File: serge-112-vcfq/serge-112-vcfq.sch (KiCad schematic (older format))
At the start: 90 parts

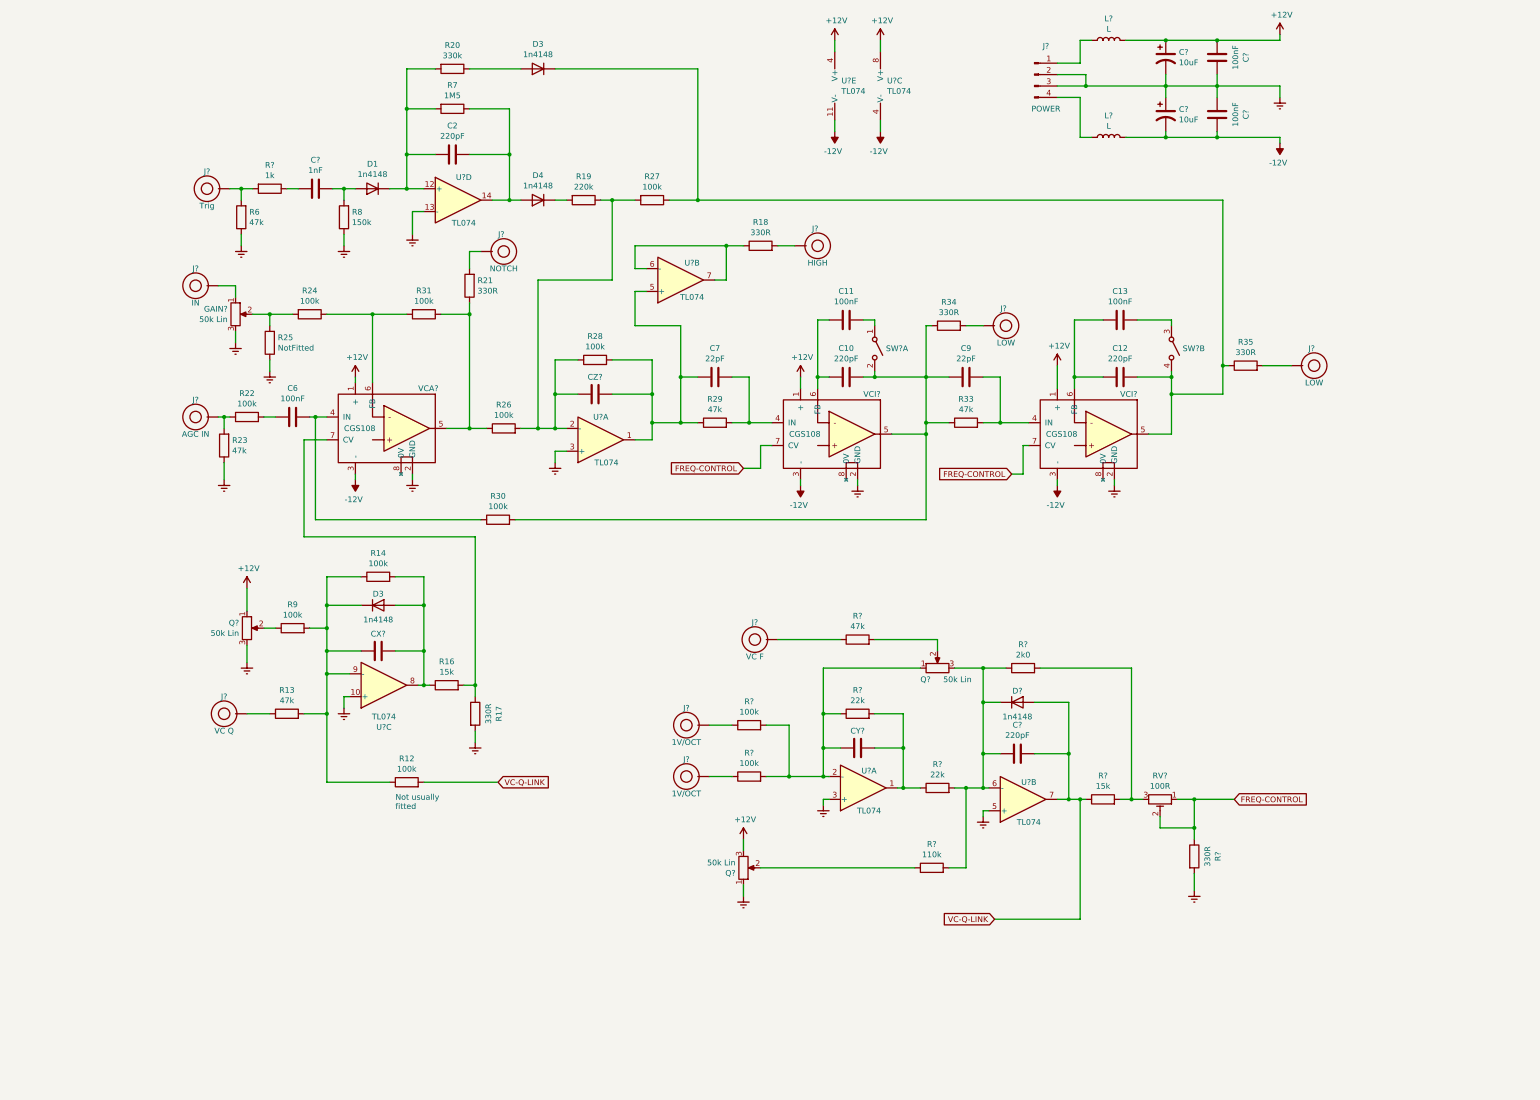
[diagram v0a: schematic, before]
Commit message: Fixing issue with serge vcfq
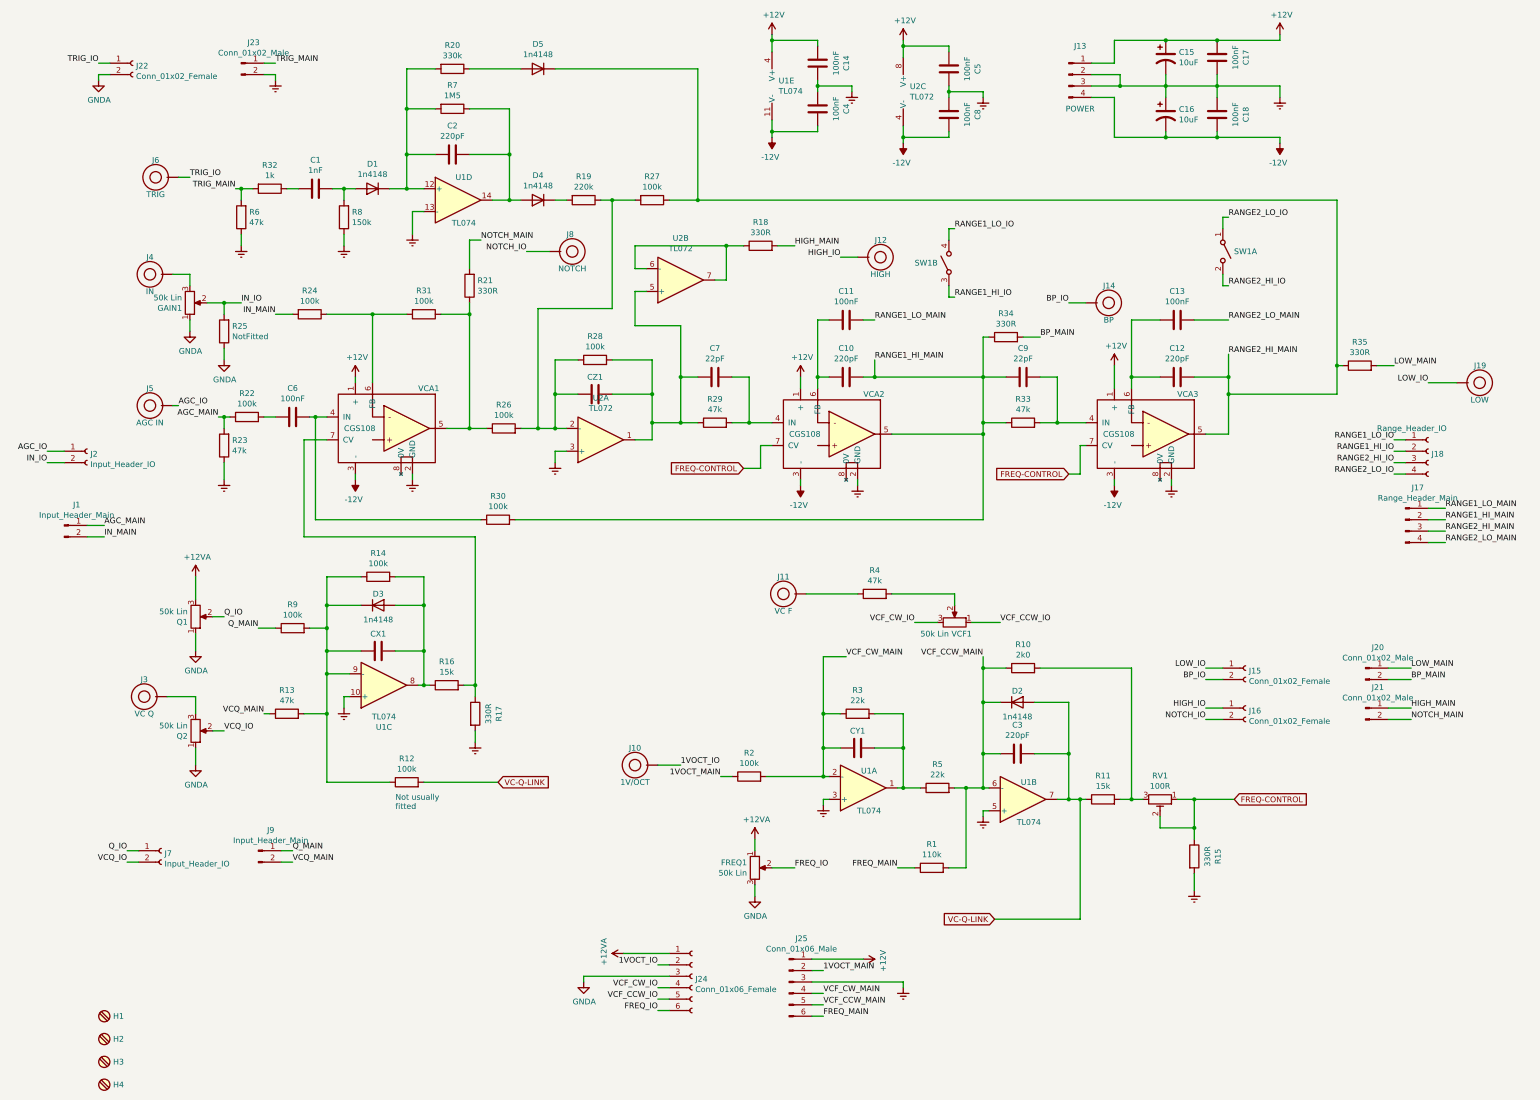
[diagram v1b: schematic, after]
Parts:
- removed J?: 1V/OCT, symbol BananaJacks:BananaJack_PanelMount
- removed L? (x2): L, symbol Device:L
- removed R?: 100k, symbol Device:R
- removed U? (x3): TL074, symbol Amplifier_Operational:TL072
- added C14, C4, C5, C8: 100nF, rumblesan-footprints:C_Rect_L7.0mm_W3.5mm_P5.00mm, symbol Device:C
- added H1, H2, H3, H4: MountingScrew_M3_Flathead, MountingHole:MountingHole_3.2mm_M3, symbol Board_Hardware:MountingScrew_M3_Flathead
- added J1, J9: Input_Header_Main, Connector_PinSocket_2.54mm:PinSocket_1x02_P2.54mm_Vertical, symbol Connector:Conn_01x02_Male
- added J15, J16, J22: Conn_01x02_Female, Connector_PinSocket_2.54mm:PinSocket_1x02_P2.54mm_Vertical, symbol Connector:Conn_01x02_Female
- added J17: Range_Header_Main, Connector_PinSocket_2.54mm:PinSocket_1x04_P2.54mm_Vertical, symbol Connector:Conn_01x04_Male
- added J18: Range_Header_IO, Connector_PinHeader_2.54mm:PinHeader_1x04_P2.54mm_Vertical, symbol Connector:Conn_01x04_Female
- added J2, J7: Input_Header_IO, Connector_PinHeader_2.54mm:PinHeader_1x02_P2.54mm_Vertical, symbol Connector:Conn_01x02_Female
- added J20, J21, J23: Conn_01x02_Male, Connector_PinHeader_2.54mm:PinHeader_1x02_P2.54mm_Vertical, symbol Connector:Conn_01x02_Male
- added J24: Conn_01x06_Female, Connector_PinSocket_2.54mm:PinSocket_1x06_P2.54mm_Vertical, symbol Connector:Conn_01x06_Female
- added J25: Conn_01x06_Male, Connector_PinHeader_2.54mm:PinHeader_1x06_P2.54mm_Vertical, symbol Connector:Conn_01x06_Male
- added Q2: 50k Lin, rumblesan-footprints:Potentiometer_Alpha_RD901F-40-00D_Single_Vertical_CircularHoles, symbol Device:R_POT
- added U2: TL072, rumblesan-footprints:DIP-8_W7.62mm_Socket, symbol Amplifier_Operational:TL072
- C1, C17, C18, C3: renamed from C?; footprint (none) -> rumblesan-footprints:C_Rect_L7.0mm_W3.5mm_P5.00mm
- C10, C12: footprint (none) -> rumblesan-footprints:C_Axial_L12.0mm_D5.0mm_P15.00mm_Horizontal
- C11, C13, C2, C6, C7, C9: footprint (none) -> rumblesan-footprints:C_Rect_L7.0mm_W3.5mm_P5.00mm
- C15, C16: renamed from C?; footprint (none) -> rumblesan-footprints:CP_Radial_D5.0mm_P2.50mm
- CX1: renamed from CX?; footprint (none) -> rumblesan-footprints:C_Rect_L7.0mm_W3.5mm_P5.00mm
- CY1: renamed from CY?; footprint (none) -> rumblesan-footprints:C_Rect_L7.0mm_W3.5mm_P5.00mm
- CZ1: renamed from CZ?; footprint (none) -> rumblesan-footprints:C_Rect_L7.0mm_W3.5mm_P5.00mm
- D1, D3, D4: footprint (none) -> rumblesan-footprints:Diode_THT_P7.62mm_Horizontal
- D2: renamed from D?; footprint (none) -> rumblesan-footprints:Diode_THT_P7.62mm_Horizontal
- D5: renamed from D3; footprint (none) -> rumblesan-footprints:Diode_THT_P7.62mm_Horizontal
- FREQ1, Q1, VCF1: renamed from Q?; footprint (none) -> rumblesan-footprints:Potentiometer_Alpha_RD901F-40-00D_Single_Vertical_CircularHoles
- GAIN1: renamed from GAIN?; footprint (none) -> rumblesan-footprints:Potentiometer_Alpha_RD901F-40-00D_Single_Vertical_CircularHoles
- J10, J11, J12, J19, J3, J4, J5, J8: renamed from J?; footprint (none) -> rumblesan-footprints:BananaJack_THT_JohnsonCinch_108-09
- J13: renamed from J?; footprint (none) -> rumblesan-footprints:Molex_KK-254_AE-6410-04A_1x04_P2.54mm_Vertical
- J14: renamed from J?; value LOW -> BP; footprint (none) -> rumblesan-footprints:BananaJack_THT_JohnsonCinch_108-09
- J6: renamed from J?; value Trig -> TRIG; footprint (none) -> rumblesan-footprints:BananaJack_THT_JohnsonCinch_108-09
- R1, R10, R11, R15, R2, R3, R32, R4, R5: renamed from R?; footprint (none) -> rumblesan-footprints:Resistor_THT_L6.3mm_D2.5mm_P10.16mm_Horizontal
- R12, R13, R14, R16, R17, R18, R19, R20, R21, R22, R23, R24, R25, R26, R27, R28, R29, R30, R31, R33, R34, R35, R6, R7, R8, R9: footprint (none) -> rumblesan-footprints:Resistor_THT_L6.3mm_D2.5mm_P10.16mm_Horizontal
- RV1: renamed from RV?; footprint (none) -> rumblesan-footprints:Potentiometer_THT_Bourns_3306P_Vertical
- SW1: renamed from SW?; footprint (none) -> rumblesan-footprints:SW_NKK_M2021SS1W03
- U1: renamed from U?; footprint (none) -> rumblesan-footprints:DIP-14_W7.62mm_Socket
- VCA1: renamed from VCA?; footprint (none) -> rumblesan-footprints:Serge_GainCell_Vertical
- VCA2, VCA3: renamed from VCI?; footprint (none) -> rumblesan-footprints:Serge_GainCell_Vertical
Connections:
- net +12V: now also J13.1 (Pin_1), C14.2, C5.2, J25.1 (Pin_1), U2.8 (V+); no longer FREQ1.3, Q1.1
- net -12V: now also J13.4 (Pin_4), C4.1, C8.1, U2.4 (V-)
- net GNDREF: now also C14.1, C4.2, C5.1, C8.2, J23.2 (Pin_2), J25.3 (Pin_3), U2.3 (+); no longer FREQ1.1, GAIN1.3, Q1.3, R25.1
- net TRIG_MAIN: now reaches R32.2, R6.2
- net TRIG_MAIN: now also J23.1 (Pin_1); no longer J6.1
- net at CZ1.2, R19.1, R26.2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: now also U2.2 (-)
- net RANGE2_HI_MAIN: now reaches C12.1, D5.1 (K), R27.1, R35.1, VCA3.5
- net RANGE2_HI_MAIN: now also J17.3 (Pin_3); no longer SW1.4 (B)
- net at J4.1: now also GAIN1.3; no longer GAIN1.1
- net IN_IO: now reaches GAIN1.2, R25.2
- net IN_IO: now also J2.2 (Pin_2); no longer R24.2
- net AGC_MAIN: now reaches R22.1, R23.2
- net AGC_MAIN: now also J1.1 (Pin_1); no longer J5.1
- net NOTCH_IO: now reaches J8.1
- net NOTCH_IO: now also J16.2 (Pin_2); no longer R21.2
- net at C7.2, CZ1.1, R28.2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: now also U2.1, U2.5 (+)
- net RANGE1_HI_MAIN: now reaches C10.1, C9.2, R30.2, R33.1, R34.1, VCA2.5
- net RANGE1_HI_MAIN: now also J17.2 (Pin_2); no longer SW1.2 (B)
- net RANGE1_HI_IO: now reaches SW1.3 (A)
- net RANGE1_HI_IO: now also J18.2 (Pin_2); no longer C13.1
- net RANGE1_LO_MAIN: now reaches C11.1
- net RANGE1_LO_MAIN: now also J17.1 (Pin_1); no longer SW1.1 (A)
- net LOW_IO: now reaches J19.1
- net LOW_IO: now also J15.1 (Pin_1); no longer R35.2
- net BP_IO: now reaches J14.1
- net BP_IO: now also J15.2 (Pin_2); no longer R34.2
- net at R18.1: now also U2.6 (-), U2.7
- net HIGH_IO: now reaches J12.1
- net HIGH_IO: now also J16.1 (Pin_1); no longer R18.2
- net Q_IO: now reaches Q1.2
- net Q_IO: now also J7.1 (Pin_1); no longer R9.1
- net at J3.1: now also Q2.3; no longer R13.1
- net VCF_CW_MAIN: now reaches CY1.2, R2.2, R3.1, U1.2 (-)
- net VCF_CW_MAIN: now also J25.4 (Pin_4); no longer VCF1.1
- net 1VOCT_IO: now reaches J10.1
- net 1VOCT_IO: now also J24.2 (Pin_2); no longer R2.1
- net VCF_CCW_MAIN: now reaches C3.2, D2.1 (K), R1.2, R10.1, R5.2, U1.6 (-)
- net VCF_CCW_MAIN: now also J25.5 (Pin_5); no longer VCF1.3
- net FREQ_IO: now reaches FREQ1.2
- net FREQ_IO: now also J24.6 (Pin_6); no longer R1.1
- new net +12VA: FREQ1.1, J24.1 (Pin_1), Q1.3
- new net 1VOCT_MAIN: J25.2 (Pin_2), R2.1
- new net AGC_IO: J2.1 (Pin_1), J5.1
- new net BP_MAIN: J20.2 (Pin_2), R34.2
- new net FREQ_MAIN: J25.6 (Pin_6), R1.1
- new net GNDA: FREQ1.3, GAIN1.1, J22.2 (Pin_2), J24.3 (Pin_3), Q1.1, Q2.1, R25.1
- new net HIGH_MAIN: J21.1 (Pin_1), R18.2
- new net IN_MAIN: J1.2 (Pin_2), R24.2
- new net LOW_MAIN: J20.1 (Pin_1), R35.2
- new net NOTCH_MAIN: J21.2 (Pin_2), R21.2
- new net Q_MAIN: J9.1 (Pin_1), R9.1
- new net RANGE1_LO_IO: J18.1 (Pin_1), SW1.4 (B)
- new net RANGE2_HI_IO: J18.3 (Pin_3), SW1.2 (B)
- new net RANGE2_LO_IO: J18.4 (Pin_4), SW1.1 (A)
- new net RANGE2_LO_MAIN: C13.1, J17.4 (Pin_4)
- new net TRIG_IO: J22.1 (Pin_1), J6.1
- new net VCF_CCW_IO: J24.5 (Pin_5), VCF1.1
- new net VCF_CW_IO: J24.4 (Pin_4), VCF1.3
- new net VCQ_IO: J7.2 (Pin_2), Q2.2
- new net VCQ_MAIN: J9.2 (Pin_2), R13.1
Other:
- moved on the sheet: C12, C13, C9, FREQ1, GAIN1, J10, J11, J12, J13, J14, J19, J3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
